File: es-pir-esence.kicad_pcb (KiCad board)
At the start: 2 copper layers, 37.8 x 27.4 mm, 21 parts, among them J1 UART, J2 5V_IN, J3 PIR, SW1 RESET, SW2 BOOT_SEL, U1 ESP-07, U2 AMS1117

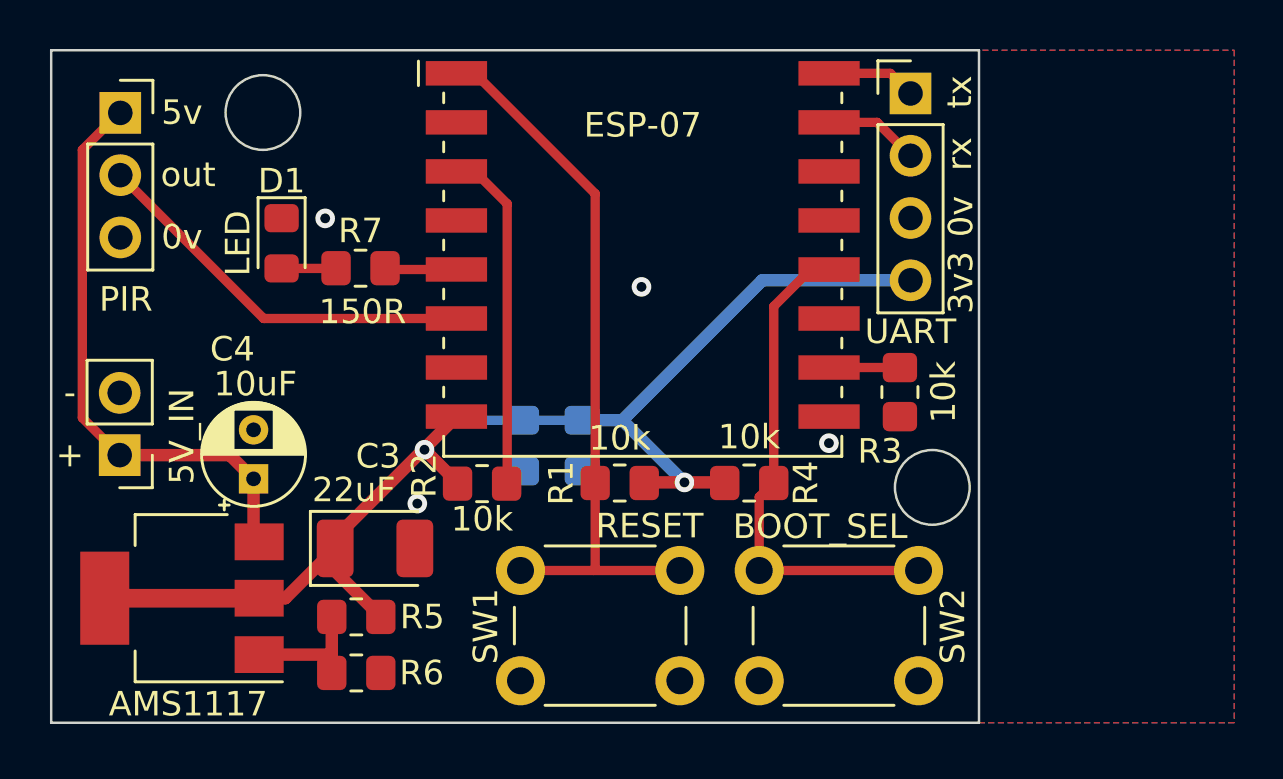
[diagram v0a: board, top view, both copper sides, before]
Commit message: Improve high frequency response of PCB
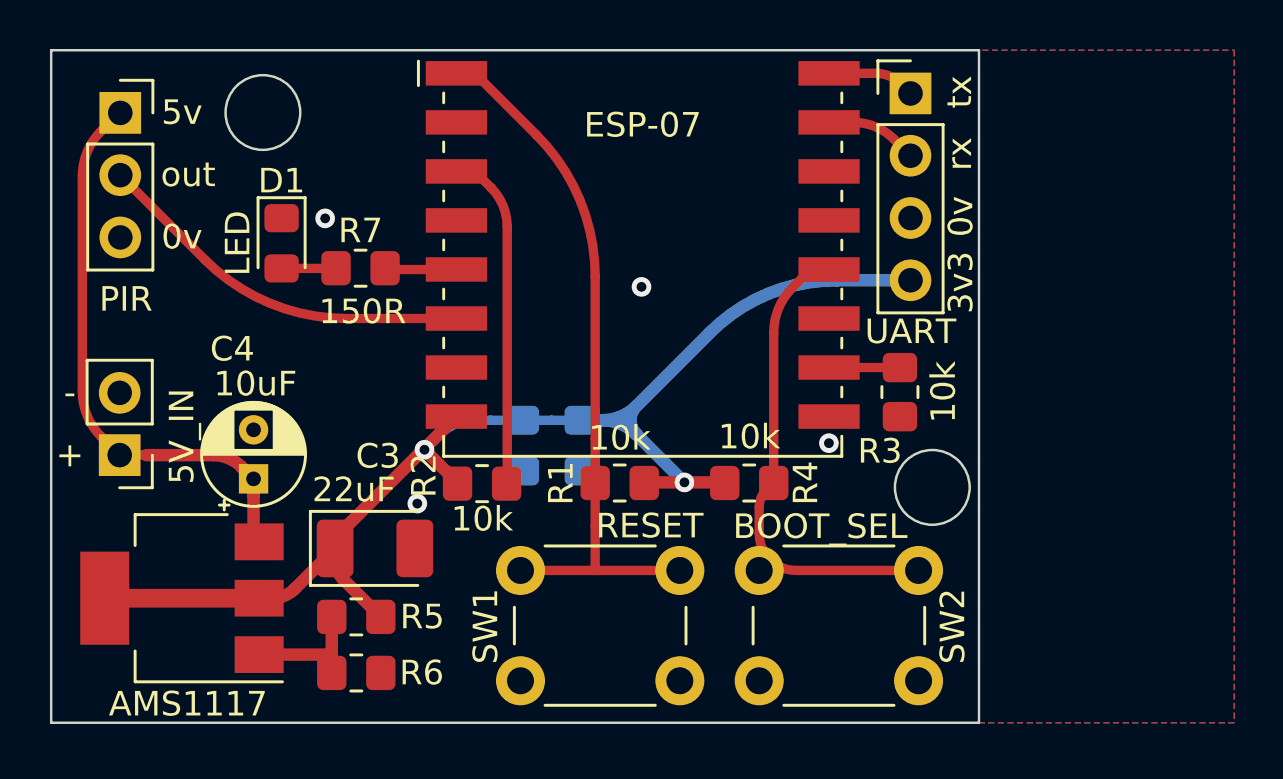
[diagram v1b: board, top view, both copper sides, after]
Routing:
- net +3V3: track 52.7 -> 54.4 mm
- net BOOT: track 20.4 -> 19.4 mm
- net +5V: track 23.9 -> 23.4 mm
